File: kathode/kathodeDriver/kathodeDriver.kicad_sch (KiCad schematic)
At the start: 206 parts, among them Q1 Q_NPN_BEC, Q10 Q_NPN_BEC, Q11 Q_NPN_BEC, Q12 Q_NPN_BEC, Q13 Q_NPN_BEC, Q14 Q_NPN_BEC, Q15 Q_NPN_BEC, Q16 Q_NPN_BEC, Q17 Q_NPN_BEC, Q18 Q_NPN_BEC, Q19 Q_NPN_BEC, Q2 Q_NPN_BEC, Q20 Q_NPN_BEC, Q21 Q_NPN_BEC, Q22 Q_NPN_BEC, Q23 Q_NPN_BEC, Q24 Q_NPN_BEC, Q25 Q_NPN_BEC, Q26 Q_NPN_BEC, Q27 Q_NPN_BEC, Q28 Q_NPN_BEC, Q29 Q_NPN_BEC, Q3 Q_NPN_BEC, Q30 Q_NPN_BEC, Q31 Q_NPN_BEC, Q32 Q_NPN_BEC, Q33 Q_NPN_BEC, Q34 Q_NPN_BEC, Q35 Q_NPN_BEC, Q36 Q_NPN_BEC, Q37 Q_NPN_BEC, Q38 Q_NPN_BEC, Q39 Q_NPN_BEC, Q4 Q_NPN_BEC, Q40 Q_NPN_BEC, Q41 Q_NPN_BEC, Q42 Q_NPN_BEC, Q43 Q_NPN_BEC, Q44 Q_NPN_BEC, Q45 Q_NPN_BEC, Q46 Q_NPN_BEC, Q47 Q_NPN_BEC, Q48 Q_NPN_BEC, Q49 Q_NPN_BEC, Q5 Q_NPN_BEC, Q50 Q_NPN_BEC, Q51 Q_NPN_BEC, Q52 Q_NPN_BEC, Q53 Q_NPN_BEC, Q54 Q_NPN_BEC, Q55 Q_NPN_BEC, Q56 Q_NPN_BEC, Q57 Q_NPN_BEC, Q58 Q_NPN_BEC, Q59 Q_NPN_BEC, Q6 Q_NPN_BEC, Q60 Q_NPN_BEC, Q61 Q_NPN_BEC, Q62 Q_NPN_BEC, Q63 Q_NPN_BEC, Q64 Q_NPN_BEC, Q7 Q_NPN_BEC, Q8 Q_NPN_BEC, Q9 Q_NPN_BEC, U1 4017, U11 4017, U13 4017, U15 4017, U2 4081, U3 4017, U4 4081, U5 4017, U6 74AUP1G32, U7 4017, U9 4017

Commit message: Finished the transistor grid
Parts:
- removed unit 4 of U4
- added C1, C10, C2, C3, C4, C5, C6, C7, C8, C9: 1uF, symbol Device:C
- added D1, D2: LED, symbol Device:LED
- added J1: Conn_01x04, symbol Connector_Generic:Conn_01x04
- added J2: Conn_01x02, symbol Connector_Generic:Conn_01x02
- added J3, J4: Conn_01x32, symbol Connector_Generic:Conn_01x32
- added R1: 100K, symbol Device:R
- added R2: 1K, symbol Device:R
- renumbered Q34 to Q1, Q39 to Q10, Q40 to Q11, Q19 to Q12, Q20 to Q13, Q10 to Q14, Q2 to Q15, Q37 to Q16, Q42 to Q17, Q43 to Q18, Q44 to Q19, Q35 to Q2, Q21 to Q20, Q22 to Q21, Q11 to Q22, Q3 to Q23, Q41 to Q24, Q46 to Q25, Q47 to Q26, Q48 to Q27, Q23 to Q28, Q24 to Q29, Q36 to Q3, Q12 to Q30, Q4 to Q31, Q45 to Q32, Q50 to Q33, Q51 to Q34, Q52 to Q35, Q25 to Q36, Q26 to Q37, Q13 to Q38, Q5 to Q39, Q17 to Q4, Q49 to Q40, Q54 to Q41, Q55 to Q42, Q56 to Q43, Q27 to Q44, Q28 to Q45, Q14 to Q46, Q6 to Q47, Q53 to Q48, Q58 to Q49, Q18 to Q5, Q59 to Q50, Q60 to Q51, Q29 to Q52, Q30 to Q53, Q15 to Q54, Q7 to Q55, Q57 to Q56, Q62 to Q57, Q63 to Q58, Q64 to Q59, Q9 to Q6, Q31 to Q60, Q32 to Q61, Q16 to Q62, Q8 to Q63, Q61 to Q64, Q1 to Q7, Q33 to Q8, Q38 to Q9, R65 to R10, R115 to R100, R116 to R101, R57 to R102, R58 to R103, R29 to R104, R13 to R105, R113 to R106, R118 to R107, R119 to R108, R120 to R109, R70 to R11, R59 to R110, R60 to R111, R30 to R112, R14 to R113, R117 to R114, R122 to R115, R123 to R116, R124 to R117, R61 to R118, R62 to R119, R71 to R12, R31 to R120, R15 to R121, R121 to R122, R126 to R123, R127 to R124, R128 to R125, R63 to R126, R64 to R127, R32 to R128, R16 to R129, R72 to R13, R125 to R130, R35 to R14, R36 to R15, R18 to R16, R2 to R17, R69 to R18, R74 to R19, R75 to R20, R76 to R21, R37 to R22, R38 to R23, R19 to R24, R3 to R25, R73 to R26, R78 to R27, R79 to R28, R80 to R29, R66 to R3, R39 to R30, R40 to R31, R20 to R32, R4 to R33, R77 to R34, R82 to R35, R83 to R36, R84 to R37, R41 to R38, R42 to R39, R67 to R4, R21 to R40, R5 to R41, R81 to R42, R86 to R43, R87 to R44, R88 to R45, R43 to R46, R44 to R47, R22 to R48, R6 to R49, R68 to R5, R85 to R50, R90 to R51, R91 to R52, R92 to R53, R45 to R54, R46 to R55, R23 to R56, R7 to R57, R89 to R58, R94 to R59, R33 to R6, R95 to R60, R96 to R61, R47 to R62, R48 to R63, R24 to R64, R8 to R65, R93 to R66, R98 to R67, R99 to R68, R100 to R69, R34 to R7, R49 to R70, R50 to R71, R25 to R72, R9 to R73, R97 to R74, R102 to R75, R103 to R76, R104 to R77, R51 to R78, R52 to R79, R17 to R8, R26 to R80, R10 to R81, R101 to R82, R106 to R83, R107 to R84, R108 to R85, R53 to R86, R54 to R87, R27 to R88, R11 to R89, R1 to R9, R105 to R90, R110 to R91, R111 to R92, R112 to R93, R55 to R94, R56 to R95, R28 to R96, R12 to R97, R109 to R98, R114 to R99, U6 to U1, U13 to U10, U15 to U11, U1 to U2, U2 to U3, U3 to U5, U5 to U6, U9 to U8, U11 to U9
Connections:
- net GND: now also U3.7 (VSS), U4.7 (VSS), C1.2, C10.2, C2.2, C3.2, C4.2, C5.2, C6.2, C7.2, C8.2, C9.2, D1.1 (K), D2.1 (K), J1.4 (Pin_4), J2.2 (Pin_2)
- net HT: now also J2.1 (Pin_1), R1.1
- net K1: no longer R23.2, R24.2, R25.2, R26.2
- net K2: no longer R39.2, R40.2, R41.2, R42.2
- net K3: no longer R55.2, R56.2, R57.2, R58.2
- net K33: now also R23.2
- net K34: now also R39.2
- net K35: now also R55.2
- net K36: now also R71.2
- net K37: now also R87.2
- net K38: now also R103.2
- net K39: now also R119.2
- net K4: no longer R71.2, R72.2, R73.2, R74.2
- net K41: now also R24.2
- net K42: now also R40.2
- net K43: now also R56.2
- net K44: now also R72.2
- net K45: now also R88.2
- net K47: now also R120.2
- net K49: now also R25.2
- net K5: no longer R87.2, R88.2, R89.2, R90.2
- net K50: now also R41.2
- net K51: now also R57.2
- net K52: now also R73.2
- net K53: now also R89.2
- net K54: now also R105.2
- net K55: now also R121.2
- net K57: now also R26.2
- net K58: now also R42.2
- net K59: now also R58.2
- net K6: no longer R103.2, R104.2, R105.2, R106.2
- net K60: now also R74.2
- net K61: now also R90.2
- net K62: now also R106.2
- net K63: now also R122.2
- net K7: no longer R119.2, R120.2, R121.2, R122.2
- net OUT_K0: now also J3.1 (Pin_1); no longer Q7.3 (C), Q8.3 (C), R17.2, R18.2
- net OUT_K1: now also J3.2 (Pin_2); no longer Q13.3 (C), Q14.3 (C), Q15.3 (C), Q16.3 (C), R31.2, R32.2, R33.2, R34.2
- net OUT_K10: now also J3.11 (Pin_11)
- net OUT_K11: now also J3.12 (Pin_12)
- net OUT_K12: now also J3.13 (Pin_13)
- net OUT_K13: now also J3.14 (Pin_14)
- net OUT_K14: now also J3.15 (Pin_15)
- net OUT_K15: now also J3.16 (Pin_16)
- net OUT_K16: now also J3.17 (Pin_17)
- net OUT_K17: now also J3.18 (Pin_18)
- net OUT_K18: now also J3.19 (Pin_19)
- net OUT_K19: now also J3.20 (Pin_20)
- net OUT_K2: now also J3.3 (Pin_3); no longer Q21.3 (C), Q22.3 (C), Q23.3 (C), Q24.3 (C), R47.2, R48.2, R49.2, R50.2
- net OUT_K20: now also J3.21 (Pin_21)
- net OUT_K21: now also J3.22 (Pin_22)
- net OUT_K22: now also J3.23 (Pin_23)
- net OUT_K23: now also J3.24 (Pin_24)
- net OUT_K24: now also J3.25 (Pin_25)
- net OUT_K25: now also J3.26 (Pin_26)
- net OUT_K26: now also J3.27 (Pin_27)
- net OUT_K27: now also J3.28 (Pin_28)
- net OUT_K28: now also J3.29 (Pin_29)
- net OUT_K29: now also J3.30 (Pin_30)
- net OUT_K3: now also J3.4 (Pin_4); no longer Q29.3 (C), Q30.3 (C), Q31.3 (C), Q32.3 (C), R63.2, R64.2, R65.2, R66.2
- net OUT_K30: now also J3.31 (Pin_31)
- net OUT_K31: now also J3.32 (Pin_32)
- net OUT_K32: now also J4.1 (Pin_1)
- net OUT_K33: now also Q13.3 (C), R31.2, J4.2 (Pin_2)
- net OUT_K34: now also Q21.3 (C), R47.2, J4.3 (Pin_3)
- net OUT_K35: now also Q29.3 (C), R63.2, J4.4 (Pin_4)
- net OUT_K36: now also Q37.3 (C), R79.2, J4.5 (Pin_5)
- net OUT_K37: now also Q45.3 (C), R95.2, J4.6 (Pin_6)
- net OUT_K38: now also Q53.3 (C), R111.2, J4.7 (Pin_7)
- net OUT_K39: now also Q61.3 (C), R127.2, J4.8 (Pin_8)
- net OUT_K4: now also J3.5 (Pin_5); no longer Q37.3 (C), Q38.3 (C), Q39.3 (C), Q40.3 (C), R79.2, R80.2, R81.2, R82.2
- net OUT_K40: now also J4.9 (Pin_9)
- net OUT_K41: now also Q14.3 (C), R32.2, J4.10 (Pin_10)
- net OUT_K42: now also Q22.3 (C), R48.2, J4.11 (Pin_11)
- net OUT_K43: now also Q30.3 (C), R64.2, J4.12 (Pin_12)
- net OUT_K44: now also Q38.3 (C), R80.2, J4.13 (Pin_13)
- net OUT_K45: now also Q46.3 (C), R96.2, J4.14 (Pin_14)
- net OUT_K46: now also Q54.3 (C), R112.2, J4.15 (Pin_15)
- net OUT_K47: now also J4.16 (Pin_16)
- net OUT_K48: now also Q62.3 (C), Q7.3 (C), R128.2, R17.2, J4.17 (Pin_17)
- net OUT_K49: now also Q15.3 (C), R33.2, J4.18 (Pin_18)
- net OUT_K5: now also J3.6 (Pin_6); no longer Q45.3 (C), Q46.3 (C), Q47.3 (C), Q48.3 (C), R95.2, R96.2, R97.2, R98.2
- net OUT_K50: now also Q23.3 (C), R49.2, J4.19 (Pin_19)
- net OUT_K51: now also Q31.3 (C), R65.2, J4.20 (Pin_20)
- net OUT_K52: now also Q39.3 (C), R81.2, J4.21 (Pin_21)
- net OUT_K53: now also Q47.3 (C), R97.2, J4.22 (Pin_22)
- net OUT_K54: now also Q55.3 (C), R113.2, J4.23 (Pin_23)
- net OUT_K55: now also Q63.3 (C), R129.2, J4.24 (Pin_24)
- net OUT_K56: now also Q8.3 (C), R18.2, J4.25 (Pin_25)
- net OUT_K57: now also Q16.3 (C), R34.2, J4.26 (Pin_26)
- net OUT_K58: now also Q24.3 (C), R50.2, J4.27 (Pin_27)
- net OUT_K59: now also Q32.3 (C), R66.2, J4.28 (Pin_28)
- net OUT_K6: now also J3.7 (Pin_7); no longer Q53.3 (C), Q54.3 (C), Q55.3 (C), Q56.3 (C), R111.2, R112.2, R113.2, R114.2
- net OUT_K60: now also Q40.3 (C), R82.2, J4.29 (Pin_29)
- net OUT_K61: now also Q48.3 (C), R98.2, J4.30 (Pin_30)
- net OUT_K62: now also Q56.3 (C), R114.2, J4.31 (Pin_31)
- net OUT_K63: now also Q64.3 (C), R130.2, J4.32 (Pin_32)
- net OUT_K7: now also J3.8 (Pin_8); no longer Q61.3 (C), Q62.3 (C), Q63.3 (C), Q64.3 (C), R127.2, R128.2, R129.2, R130.2
- net OUT_K8: now also J3.9 (Pin_9)
- net OUT_K9: now also J3.10 (Pin_10)
- net RESET_COUNT: now also J1.3 (Pin_3)
- net VCC: now also U3.14 (VDD), U4.14 (VDD), C1.1, C10.1, C2.1, C3.1, C4.1, C5.1, C6.1, C7.1, C8.1, C9.1, J1.1 (Pin_1), R2.1
- net INPUT_CLK: now reaches U2.14 (CLK), U3.2
- net INPUT_CLK: now also J1.2 (Pin_2)
- new net: D1.2 (A), R1.2
- new net: D2.2 (A), R2.2
- new net uK46: R104.2
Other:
- moved on the sheet: U4E

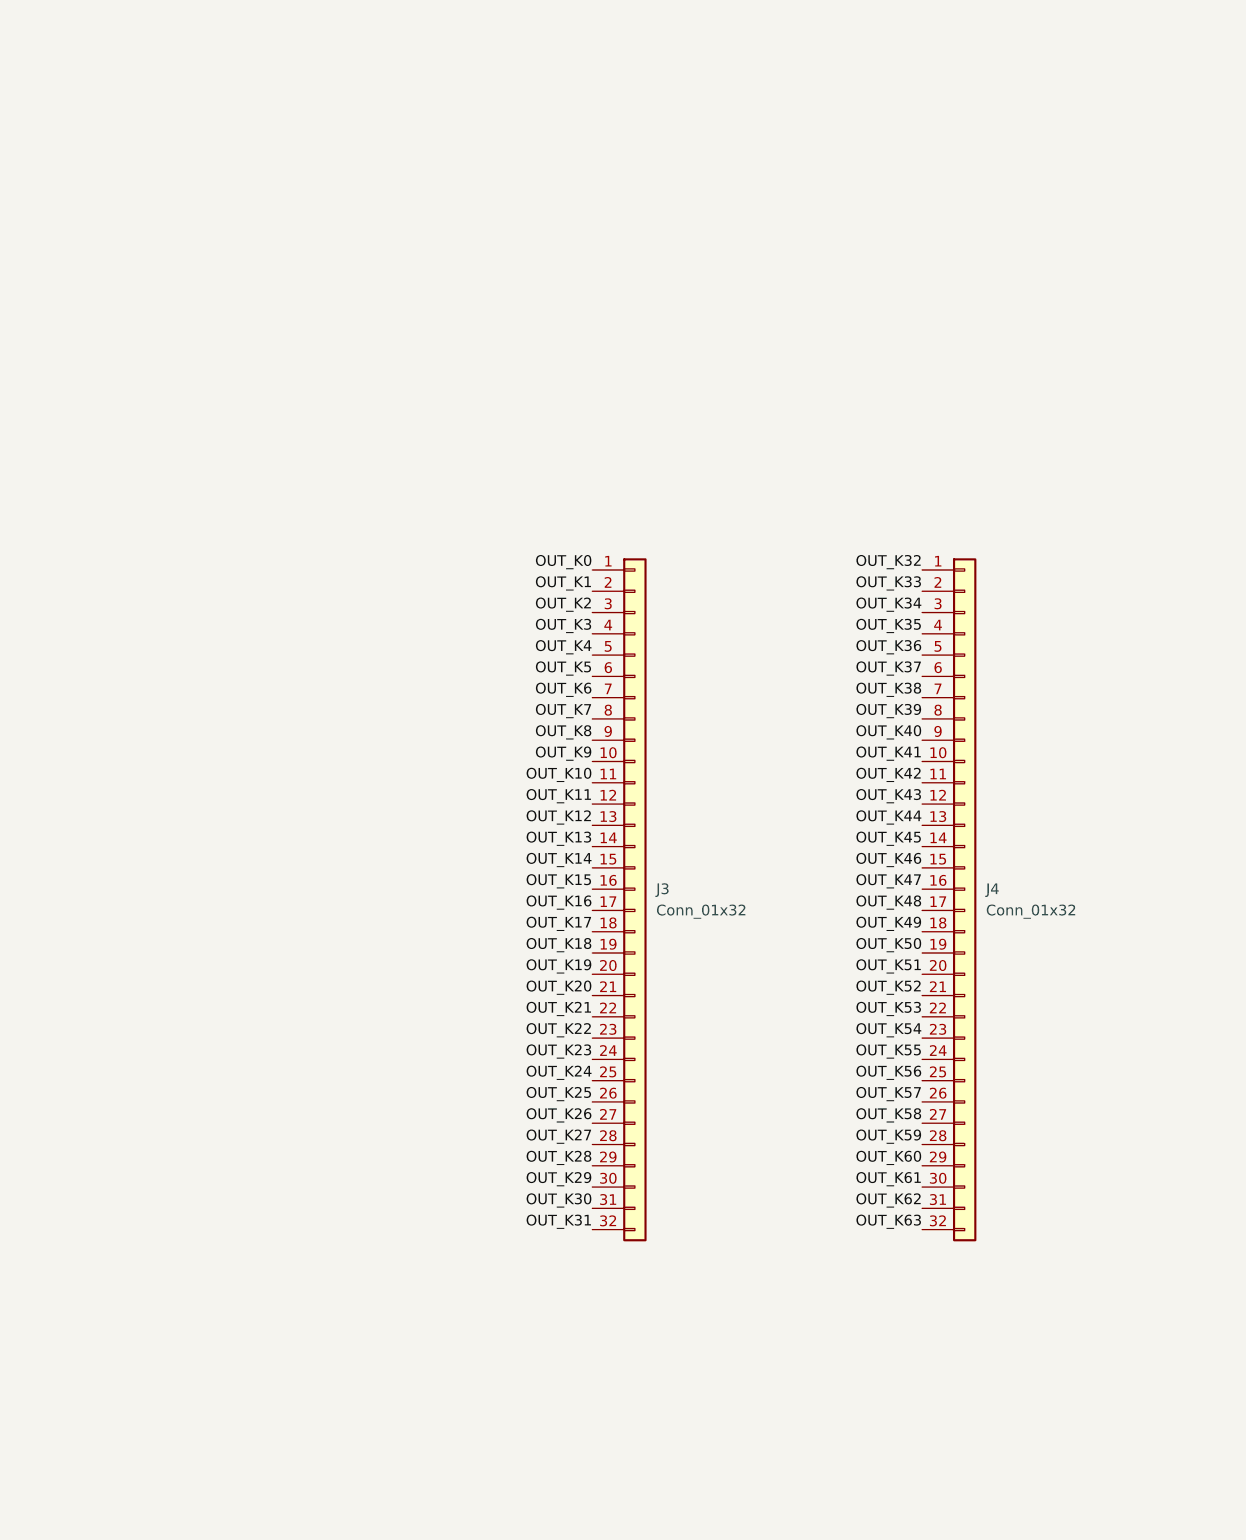
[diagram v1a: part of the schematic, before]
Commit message: Added footprint for board
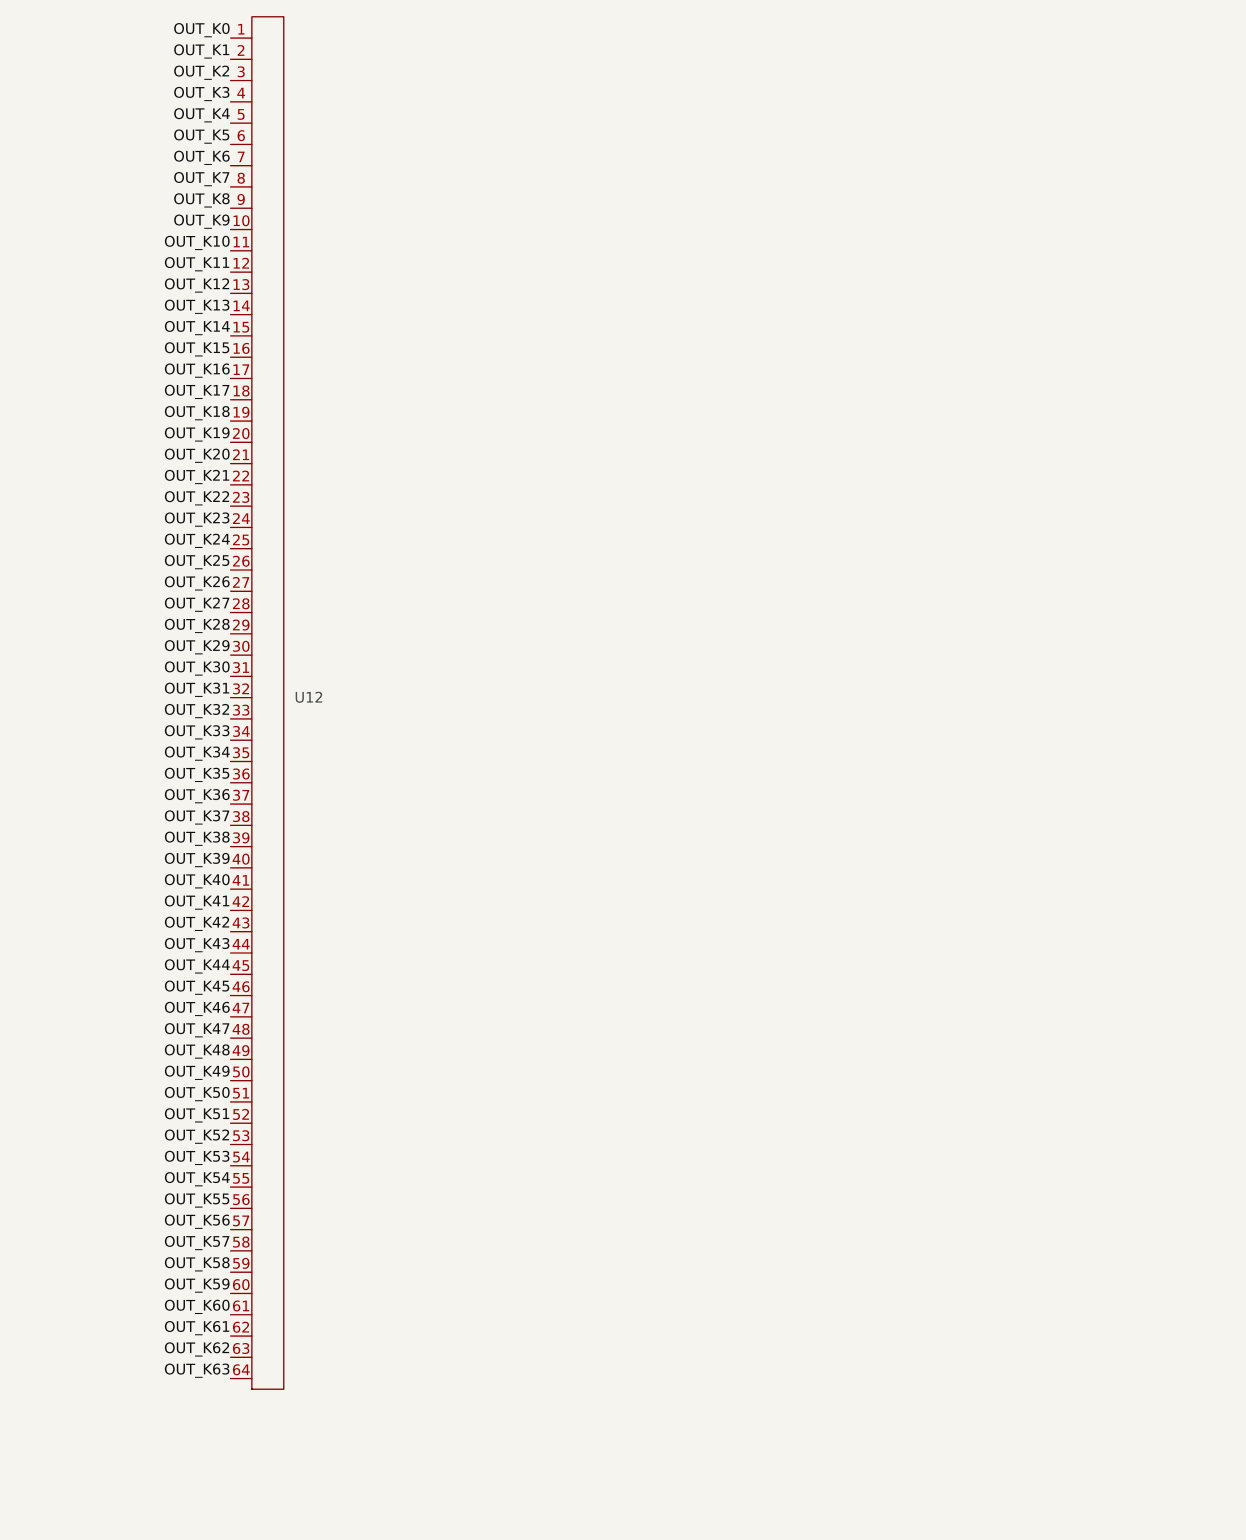
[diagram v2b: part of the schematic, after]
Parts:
- removed J3, J4: Conn_01x32, symbol Connector_Generic:Conn_01x32
- added U12: ~, IGG1:IGG1, symbol IGG1:IGG1-64
- C1, C10, C2, C3, C4, C5, C6, C7, C8, C9: footprint (none) -> Capacitor_SMD:C_0603_1608Metric
- D1, D2: footprint (none) -> LED_SMD:LED_0603_1608Metric
- J1: footprint (none) -> Connector_JST:JST_XH_B4B-XH-AM_1x04_P2.50mm_Vertical
- J2: footprint (none) -> Connector_JST:JST_XH_B2B-XH-AM_1x02_P2.50mm_Vertical
- JP1: footprint (none) -> Jumper:SolderJumper-2_P1.3mm_Bridged_RoundedPad1.0x1.5mm
- R1: footprint (none) -> Resistor_SMD:R_0603_1608Metric; LCSC (none) -> C25803
- R10, R100, R101, R102, R103, R104, R105, R106, R115, R116, R117, R118, R119, R120, R121, R122, R19, R20, R21, R22, R23, R24, R25, R26, R3, R35, R36, R37, R38, R39, R4, R40, R41, R42, R5, R51, R52, R53, R54, R55, R56, R57, R58, R6, R67, R68, R69, R7, R70, R71, R72, R73, R74, R8, R83, R84, R85, R86, R87, R88, R89, R9, R90, R99: footprint Resistors_SMD:R_1206 -> Resistor_SMD:R_0603_1608Metric; LCSC (none) -> C25804
- R107, R108, R109, R11, R110, R111, R112, R113, R114, R12, R123, R124, R125, R126, R127, R128, R129, R13, R130, R14, R15, R16, R17, R18, R27, R28, R29, R30, R31, R32, R33, R34, R43, R44, R45, R46, R47, R48, R49, R50, R59, R60, R61, R62, R63, R64, R65, R66, R75, R76, R77, R78, R79, R80, R81, R82, R91, R92, R93, R94, R95, R96, R97, R98: footprint Resistors_SMD:R_1206 -> Resistor_SMD:R_0805_2012Metric; LCSC (none) -> C17556
- R2: footprint (none) -> Resistor_SMD:R_0603_1608Metric; LCSC (none) -> C21190
- TP1, TP2: footprint (none) -> TestPoint:TestPoint_Loop_D2.50mm_Drill1.0mm
- U1: footprint (none) -> Package_TO_SOT_SMD:SOT-23-5; LCSC (none) -> C7470
- U10, U11, U2, U5, U6, U7, U8, U9: footprint (none) -> Package_SO:SOP-16_4.4x10.4mm_P1.27mm
- U3, U4: footprint (none) -> Package_SO:SOIC-14_3.9x8.7mm_P1.27mm
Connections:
- net OUT_K0: now also U12.1
- net OUT_K1: now also U12.2
- net OUT_K10: now also U12.11
- net OUT_K11: now also U12.12
- net OUT_K12: now also U12.13
- net OUT_K13: now also U12.14
- net OUT_K14: now also U12.15
- net OUT_K15: now also U12.16
- net OUT_K16: now also U12.17
- net OUT_K17: now also U12.18
- net OUT_K18: now also U12.19
- net OUT_K19: now also U12.20
- net OUT_K2: now also U12.3
- net OUT_K20: now also U12.21
- net OUT_K21: now also U12.22
- net OUT_K22: now also U12.23
- net OUT_K23: now also U12.24
- net OUT_K24: now also U12.25
- net OUT_K25: now also U12.26
- net OUT_K26: now also U12.27
- net OUT_K27: now also U12.28
- net OUT_K28: now also U12.29
- net OUT_K29: now also U12.30
- net OUT_K3: now also U12.4
- net OUT_K30: now also U12.31
- net OUT_K31: now also U12.32
- net OUT_K32: now also U12.33
- net OUT_K33: now also U12.34
- net OUT_K34: now also U12.35
- net OUT_K35: now also U12.36
- net OUT_K36: now also U12.37
- net OUT_K37: now also U12.38
- net OUT_K38: now also U12.39
- net OUT_K39: now also U12.40
- net OUT_K4: now also U12.5
- net OUT_K40: now also U12.41
- net OUT_K41: now also U12.42
- net OUT_K42: now also U12.43
- net OUT_K43: now also U12.44
- net OUT_K44: now also U12.45
- net OUT_K45: now also U12.46
- net OUT_K46: now also U12.47
- net OUT_K47: now also U12.48
- net OUT_K48: now also U12.49
- net OUT_K49: now also U12.50
- net OUT_K5: now also U12.6
- net OUT_K50: now also U12.51
- net OUT_K51: now also U12.52
- net OUT_K52: now also U12.53
- net OUT_K53: now also U12.54
- net OUT_K54: now also U12.55
- net OUT_K55: now also U12.56
- net OUT_K56: now also U12.57
- net OUT_K57: now also U12.58
- net OUT_K58: now also U12.59
- net OUT_K59: now also U12.60
- net OUT_K6: now also U12.7
- net OUT_K60: now also U12.61
- net OUT_K61: now also U12.62
- net OUT_K62: now also U12.63
- net OUT_K63: now also U12.64
- net OUT_K7: now also U12.8
- net OUT_K8: now also U12.9
- net OUT_K9: now also U12.10

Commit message: Started work on layout
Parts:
- C1, C10, C2, C3, C4, C5, C6, C7, C8, C9: LCSC (none) -> C15849
- D1: LCSC (none) -> C72038
- D2: LCSC (none) -> C2286
- Q1, Q10, Q11, Q12, Q13, Q14, Q15, Q16, Q17, Q18, Q19, Q2, Q20, Q21, Q22, Q23, Q24, Q25, Q26, Q27, Q28, Q29, Q3, Q30, Q31, Q32, Q33, Q34, Q35, Q36, Q37, Q38, Q39, Q4, Q40, Q41, Q42, Q43, Q44, Q45, Q46, Q47, Q48, Q49, Q5, Q50, Q51, Q52, Q53, Q54, Q55, Q56, Q57, Q58, Q59, Q6, Q60, Q61, Q62, Q63, Q64, Q7, Q8, Q9: footprint TO_SOT_Packages_SMD:SOT-23 -> Package_TO_SOT_SMD:SOT-23; LCSC (none) -> C151355

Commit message: Lots of routing done
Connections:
- net OUT_K47: now also Q62.3 (C), R128.2
- net OUT_K48: no longer Q62.3 (C), R128.2
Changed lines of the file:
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@@
 		)
 	)
-	(label "OUT_K48"
+	(label "OUT_K47"
 		(at 476.25 259.08 180)
 		(fields_autoplaced yes)

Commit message: Finished the kathode driver, onto the anodes
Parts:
- added C11: 1uF, Capacitor_SMD:C_0603_1608Metric, symbol Device:C
- added H1, H2: MountingHole, Mounting_Wuerth:Mounting_Wuerth_WA-SMSI-M3_H2mm_9774020360, symbol Mechanical:MountingHole
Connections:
- net uK46 is gone; now on net K46: R104.2
- net CLK: now also U3.13
- net GND: now also C11.2
- net VCC: now also C11.1
- net at U3.10: now also U8.14 (CLK); no longer U7.14 (CLK)
- net at U6.11 (Q9), U6.13 (CKEN): now also U3.12; no longer U3.8
- net at U7.11 (Q9), U7.13 (CKEN): now also U3.8; no longer U3.12
- net at U3.11: now also U7.14 (CLK); no longer U8.14 (CLK)
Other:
- moved on the sheet: U3C, U3D
